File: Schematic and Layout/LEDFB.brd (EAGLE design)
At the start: 160 x 100 mm, 25 parts, among them U1 TLV61225L

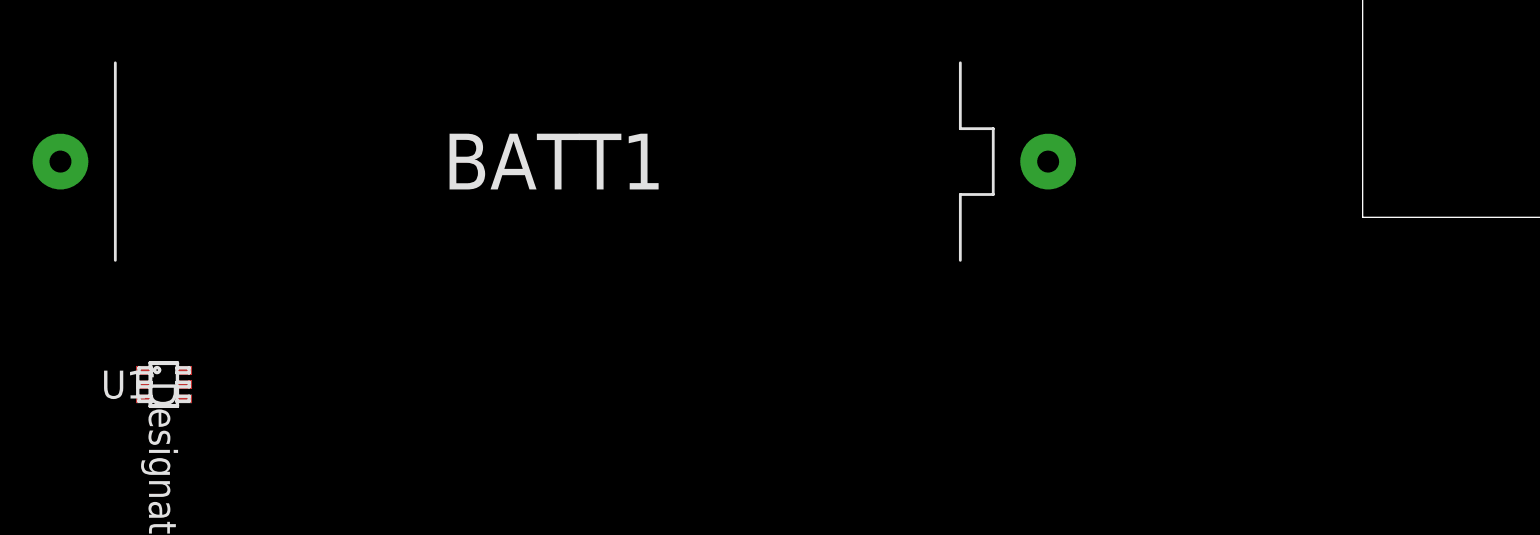
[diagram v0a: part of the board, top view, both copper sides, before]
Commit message: Added itg3701 library, added a gitignore document to ignore autosave files, added reference docs
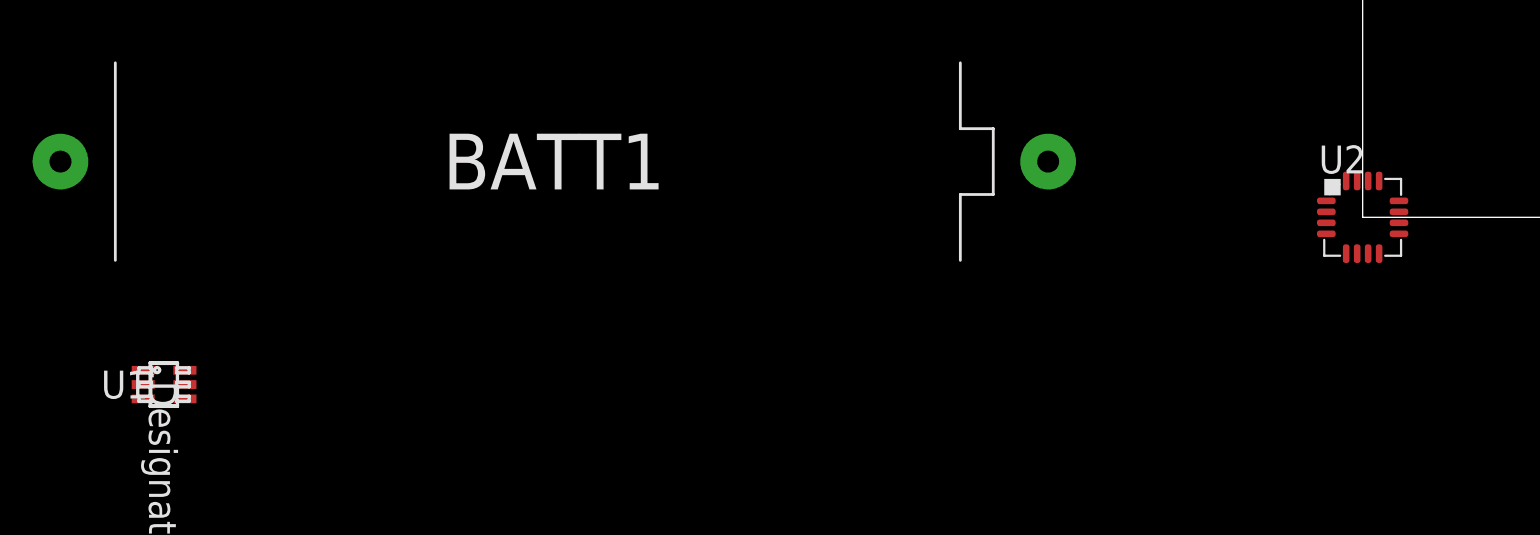
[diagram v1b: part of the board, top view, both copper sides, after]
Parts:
- added U2: ITG-37013X3MM, itg_3701:QFN-16
- U1: value TLV61225L -> TLV61225M; device TLV61225:DCK0006A_L -> TLV61225:DCK0006A_M
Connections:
- new net CS: U2.4
- new net GND_RSVD: U2.14
- new net INT: U2.10
- new net NC3: U2.13
- new net NC4: U2.15
- new net NC_RSVD: U2.5
- new net SDA/SDI: U2.1
- new net VDD: U2.9
- new net VDDIO: U2.3
- net GND: now also U2.12
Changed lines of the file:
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@@
 <setting verticaltext="up"/>
 </settings>
-<grid distance="0.05" unitdist="inch" unit="inch" style="lines" multiple="1" display="no" altdistance="0.025" altunitdist="inch" altunit="inch"/>
+<grid distance="0.5" unitdist="mm" unit="mm" style="lines" multiple="1" display="yes" altdistance="0.25" altunitdist="mm" altunit="mm"/>
 <layers>
 <layer number="1" name="Top" color="4" fill="1" visible="yes" active="yes"/>
@@
 <element name="C2" library="adafruit" package="C0805" value="10uF" x="-24.13" y="31.75"/>
 <element name="S2" library="adafruit" package="EG1218" value="" x="-33.02" y="22.86"/>
-<element name="U1" library="TLV61225" package="DCK0006A_L" value="TLV61225L" x="-54.61" y="-7.62"/>
+<element name="U1" library="TLV61225" package="DCK0006A_M" value="TLV61225M" x="-54.61" y="-7.62"/>
+<element name="U2" library="itg_3701" package="QFN-16" value="ITG-37013X3MM" x="0" y="0"/>
 </elements>
 <signals>
@@
 <contactref element="C2" pad="2"/>
 <contactref element="U1" pad="3"/>
+<contactref element="U2" pad="12"/>
+<wire x1="-55.559996875" y1="-8.27" x2="1.655" y2="0.75" width="0" layer="19" extent="1-1"/>
 <wire x1="-14.33" y1="2.54" x2="-55.559996875" y2="-8.27" width="0" layer="19" extent="1-1"/>
 <wire x1="-11.9888" y1="16.2306" x2="-14.33" y2="2.54" width="0" layer="19" extent="1-1"/>
@@
 <contactref element="U1" pad="4"/>
 </signal>
+<signal name="NC4">
+<contactref element="U2" pad="15"/>
+</signal>
+<signal name="NC_RSVD">
+<contactref element="U2" pad="5"/>
+</signal>
+<signal name="NC3">
+<contactref element="U2" pad="13"/>
+</signal>
+<signal name="GND_RSVD">
+<contactref element="U2" pad="14"/>
+</signal>
+<signal name="CS">
+<contactref element="U2" pad="4"/>
+</signal>
+<signal name="SDA/SDI">
+<contactref element="U2" pad="1"/>
+</signal>
+<signal name="VDDIO">
+<contactref element="U2" pad="3"/>
+</signal>
+<signal name="INT">
+<contactref element="U2" pad="10"/>
+</signal>
+<signal name="VDD">
+<contactref element="U2" pad="9"/>
+</signal>
 </signals>
